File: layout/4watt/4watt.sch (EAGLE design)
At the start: 51 parts, among them IC2 FT232RL, P1 FSM4JSMA-SMD, Q1 IRF7413, Q2 IRF7413, Q3 IRF7413, Q4 IRF7413, T1 BC848, T2 BC848, T3 BC848, T4 BC848, T5 BC848, T6 BC848

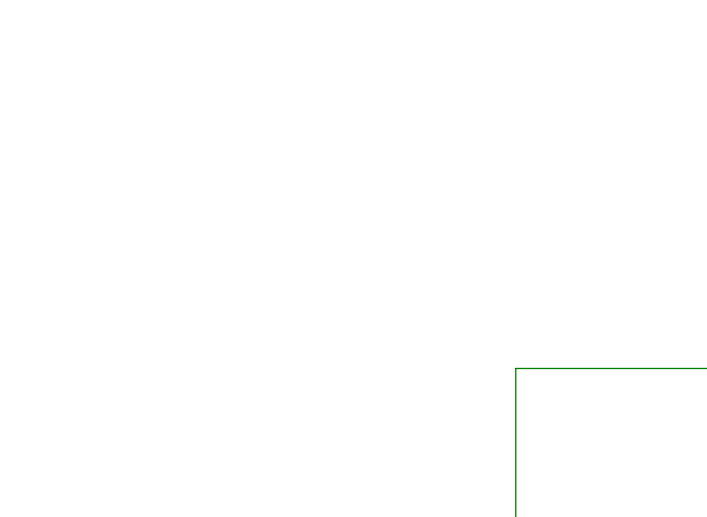
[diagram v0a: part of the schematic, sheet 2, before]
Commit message: ws28xx output and 2 additional RGBW led connectors
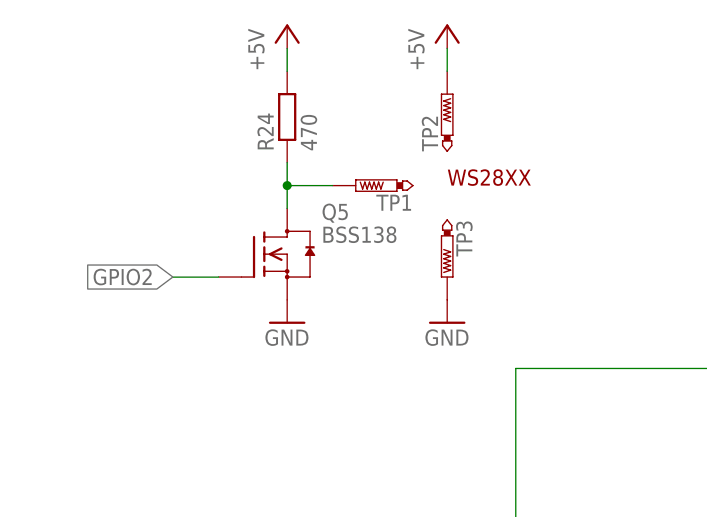
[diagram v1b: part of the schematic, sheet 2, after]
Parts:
- added Q5: BSS138, m-pad-2.1:BSS138
- added R24: 470, rcl-2:R-EU_R0603
- added TP1: PTR1B1,27, testpad:PTR1B1,27
- added TP2, TP3: PTR1B2,54, testpad:PTR1B2,54
- added X1: 1296-T10, con-leotronics:1296-T10
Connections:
- new net GPIO2: Q5.G, R21.1, U$2.GPIO2
- new net N$15: U2.PWM4, X1-2.B
- new net N$16: U2.PWM5, X1-4.B
- new net N$17: U2.PWM6, X1-6.B
- new net N$18: U2.PWM7, X1-8.B
- new net N$19: U2.PWM8, X1-1.B
- new net N$20: U2.PWM9, X1-3.B
- new net N$21: U2.PWM10, X1-5.B
- new net N$22: U2.PWM11, X1-7.B
- net +5V: now also R24.2, TP2.TP
- net GND: now also Q5.S, TP3.TP, X1-10.B, X1-9.B
- net N$6: now also Q5.D, R24.1, TP1.TP; no longer R21.1, U$2.GPIO2
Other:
- note added: "WS28XX"
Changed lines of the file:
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@@
 <part name="C9" library="rcl" deviceset="C-EU" device="C0603" value="100n"/>
 <part name="GND31" library="supply1" deviceset="GND" device=""/>
+<part name="Q5" library="m-pad-2.1" deviceset="BSS138" device=""/>
+<part name="GND32" library="supply1" deviceset="GND" device=""/>
+<part name="R24" library="rcl-2" deviceset="R-EU_" device="R0603" value="470"/>
+<part name="P+5" library="supply1" deviceset="+5V" device=""/>
+<part name="TP1" library="testpad" deviceset="PTR1" device="B1,27"/>
+<part name="TP2" library="testpad" deviceset="PTR1" device="B2,54"/>
+<part name="TP3" library="testpad" deviceset="PTR1" device="B2,54"/>
+<part name="P+7" library="supply1" deviceset="+5V" device=""/>
+<part name="GND33" library="supply1" deviceset="GND" device=""/>
+<part name="X1" library="con-leotronics" deviceset="1296-T10" device=""/>
+<part name="GND34" library="supply1" deviceset="GND" device=""/>
 </parts>
 <sheets>
@@
 <instance part="C9" gate="G$1" x="243.84" y="45.72"/>
 <instance part="GND31" gate="1" x="243.84" y="33.02"/>
+<instance part="X1" gate="-1" x="241.3" y="134.62"/>
+<instance part="X1" gate="-2" x="241.3" y="144.78"/>
+<instance part="X1" gate="-3" x="241.3" y="132.08"/>
+<instance part="X1" gate="-4" x="241.3" y="142.24"/>
+<instance part="X1" gate="-5" x="241.3" y="129.54"/>
+<instance part="X1" gate="-6" x="241.3" y="139.7"/>
+<instance part="X1" gate="-7" x="241.3" y="127"/>
+<instance part="X1" gate="-8" x="241.3" y="137.16"/>
+<instance part="X1" gate="-9" x="246.38" y="119.38"/>
+<instance part="X1" gate="-10" x="246.38" y="116.84"/>
+<instance part="GND34" gate="1" x="241.3" y="111.76"/>
 </instances>
 <busses>
@@
 <wire x1="243.84" y1="35.56" x2="243.84" y2="40.64" width="0.1524" layer="91"/>
 </segment>
+<segment>
+<pinref part="X1" gate="-10" pin="B"/>
+<pinref part="GND34" gate="1" pin="GND"/>
+<wire x1="243.84" y1="116.84" x2="241.3" y2="116.84" width="0.1524" layer="91"/>
+<wire x1="241.3" y1="116.84" x2="241.3" y2="114.3" width="0.1524" layer="91"/>
+<pinref part="X1" gate="-9" pin="B"/>
+<wire x1="243.84" y1="119.38" x2="241.3" y2="119.38" width="0.1524" layer="91"/>
+<wire x1="241.3" y1="119.38" x2="241.3" y2="116.84" width="0.1524" layer="91"/>
+<junction x="241.3" y="116.84"/>
+</segment>
 </net>
 <net name="N$12" class="0">
@@
 </segment>
 </net>
-<net name="N$6" class="0">
+<net name="GPIO2" class="0">
 <segment>
 <pinref part="U$2" gate="G$1" pin="GPIO2"/>
@@
 <pinref part="R21" gate="G$1" pin="1"/>
 <wire x1="187.96" y1="55.88" x2="187.96" y2="83.82" width="0.1524" layer="91"/>
+<wire x1="187.96" y1="55.88" x2="177.8" y2="55.88" width="0.1524" layer="91"/>
+<junction x="187.96" y="55.88"/>
+<label x="177.8" y="55.88" size="1.778" layer="95" rot="R180" xref="yes"/>
+</segment>
+</net>
+<net name="N$15" class="0">
+<segment>
+<pinref part="U2" gate="G$1" pin="PWM4"/>
+<pinref part="X1" gate="-2" pin="B"/>
+</segment>
+</net>
+<net name="N$16" class="0">
+<segment>
+<pinref part="U2" gate="G$1" pin="PWM5"/>
+<pinref part="X1" gate="-4" pin="B"/>
+</segment>
+</net>
+<net name="N$17" class="0">
+<segment>
+<pinref part="U2" gate="G$1" pin="PWM6"/>
+<pinref part="X1" gate="-6" pin="B"/>
+</segment>
+</net>
+<net name="N$18" class="0">
+<segment>
+<pinref part="U2" gate="G$1" pin="PWM7"/>
+<pinref part="X1" gate="-8" pin="B"/>
+</segment>
+</net>
+<net name="N$19" class="0">
+<segment>
+<pinref part="U2" gate="G$1" pin="PWM8"/>
+<pinref part="X1" gate="-1" pin="B"/>
+</segment>
+</net>
+<net name="N$20" class="0">
+<segment>
+<pinref part="U2" gate="G$1" pin="PWM9"/>
+<pinref part="X1" gate="-3" pin="B"/>
+</segment>
+</net>
+<net name="N$21" class="0">
+<segment>
+<pinref part="U2" gate="G$1" pin="PWM10"/>
+<pinref part="X1" gate="-5" pin="B"/>
+</segment>
+</net>
+<net name="N$22" class="0">
+<segment>
+<pinref part="U2" gate="G$1" pin="PWM11"/>
+<pinref part="X1" gate="-7" pin="B"/>
 </segment>
 </net>
@@
 <text x="154.94" y="86.36" size="1.778" layer="94">3.0V</text>
 <text x="215.9" y="86.36" size="1.778" layer="94">3.0V</text>
+<text x="53.34" y="154.94" size="1.778" layer="94">WS28XX</text>
 </plain>
 <instances>
@@
 <instance part="GND21" gate="1" x="251.46" y="48.26"/>
 <instance part="P+3" gate="1" x="134.62" y="157.48"/>
+<instance part="Q5" gate="G$1" x="33.02" y="147.32"/>
+<instance part="GND32" gate="1" x="35.56" y="139.7"/>
+<instance part="R24" gate="G$1" x="35.56" y="162.56" rot="R90"/>
+<instance part="P+5" gate="1" x="35.56" y="172.72"/>
+<instance part="TP1" gate="G$1" x="43.18" y="154.94" rot="R90"/>
+<instance part="TP2" gate="G$1" x="53.34" y="165.1"/>
+<instance part="TP3" gate="G$1" x="53.34" y="144.78" rot="R180"/>
+<instance part="P+7" gate="1" x="53.34" y="172.72"/>
+<instance part="GND33" gate="1" x="53.34" y="139.7"/>
 </instances>
 <busses>
@@
 <pinref part="GND21" gate="1" pin="GND"/>
 <wire x1="251.46" y1="58.42" x2="251.46" y2="50.8" width="0.1524" layer="91"/>
+</segment>
+<segment>
+<pinref part="Q5" gate="G$1" pin="S"/>
+<pinref part="GND32" gate="1" pin="GND"/>
+</segment>
+<segment>
+<pinref part="TP3" gate="G$1" pin="TP"/>
+<pinref part="GND33" gate="1" pin="GND"/>
 </segment>
 </net>
@@
 <pinref part="P+3" gate="1" pin="+5V"/>
 </segment>
-</net>
+<segment>
+<pinref part="R24" gate="G$1" pin="2"/>
+<pinref part="P+5" gate="1" pin="+5V"/>
+<wire x1="35.56" y1="170.18" x2="35.56" y2="167.64" width="0.1524" layer="91"/>
+</segment>
+<segment>
+<pinref part="TP2" gate="G$1" pin="TP"/>
+<pinref part="P+7" gate="1" pin="+5V"/>
+<wire x1="53.34" y1="170.18" x2="53.34" y2="167.64" width="0.1524" layer="91"/>
+</segment>
+</net>
+<net name="GPIO2" class="0">
+<segment>
+<pinref part="Q5" gate="G$1" pin="G"/>
+<wire x1="27.94" y1="144.78" x2="22.86" y2="144.78" width="0.1524" layer="91"/>
+<label x="22.86" y="144.78" size="1.778" layer="95" rot="R180" xref="yes"/>
+</segment>
+</net>
+<net name="N$6" class="0">
+<segment>
+<pinref part="R24" gate="G$1" pin="1"/>
+<pinref part="Q5" gate="G$1" pin="D"/>
+<wire x1="35.56" y1="157.48" x2="35.56" y2="154.94" width="0.1524" layer="91"/>
+<pinref part="TP1" gate="G$1" pin="TP"/>
+<wire x1="35.56" y1="154.94" x2="35.56" y2="152.4" width="0.1524" layer="91"/>
+<wire x1="35.56" y1="154.94" x2="40.64" y2="154.94" width="0.1524" layer="91"/>
+<junction x="35.56" y="154.94"/>
+</segment>
+</net>

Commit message: Bauteilbeschriftung der Platinen base und 4watt geordnet. Bestückungspläne hinzugefügt.
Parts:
- C3: value 22p -> 100n
- C4: value 22p -> 100u; device rcl:C-EUC0603 -> cap-master:CP-7343-TE-D
- C6: value 100u -> 100n; device cap-master:CP-7343-TE-D -> rcl:C-EUC0603
- C7, C8: value 100n -> 22p
- Q1: value IRF7413 -> BSS138; device transistor-fet:IRF7413 -> m-pad-2.1:BSS138
- Q5: value BSS138 -> IRF7413; device m-pad-2.1:BSS138 -> transistor-fet:IRF7413
- R10: value 3R6 -> 470; device rcl-2:R-EU_M1206 -> rcl-2:R-EU_R0603
- R16: value 3R6 -> 360; device rcl-2:R-EU_M1206 -> rcl-2:R-EU_R0603
- R18: value 360 -> 3R6; device rcl-2:R-EU_R0603 -> rcl-2:R-EU_M1206
- R19, R20, R21, R22, R23: value 10k -> 3R6; device rcl-2:R-EU_R0603 -> rcl-2:R-EU_M1206
- R24: value 470 -> 3R6; device rcl-2:R-EU_R0603 -> rcl-2:R-EU_M1206
- R5, R6, R7, R8, R9: value 3R6 -> 10k; device rcl-2:R-EU_M1206 -> rcl-2:R-EU_R0603
- TP1: value PTR1B1,27 -> PTR1B2,54; device testpad:PTR1B1,27 -> testpad:PTR1B2,54
- TP2: value PTR1B2,54 -> PTR1B1,27; device testpad:PTR1B2,54 -> testpad:PTR1B1,27
- renumbered U$2 to U$1, U$40 to X2, U2 to U1
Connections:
- net +3V3: now also C3.1, C4.+, C5.1, R3.2, R4.2, R5.2, R6.2; no longer C6.+, C7.1, C8.1, R19.2, R20.2, R21.2, R23.2
- net +5V: now also C2.1, R10.2, TP1.TP; no longer C5.1, R24.2, TP2.TP
- net GND: now also C4.-, C6.2, Q1.S, R18.1, R19.1, R20.1, R21.1, R23.1, R24.1; no longer C4.2, C6.-, Q5.S, R10.1, R11.1, R16.1, R6.1, R7.1, R8.1
- net GPIO0: now also R5.1, T1.C; no longer R23.1, T2.C
- net GPIO15: now also R9.2; no longer R22.2
- net GPIO2: now also Q1.G, R6.1; no longer Q5.G, R21.1
- net N$1: now also R7.1, T2.E; no longer R3.1, T1.E
- net N$10: now also R11.1; no longer R5.1
- net N$11: now also Q5.G, R16.2; no longer Q4.G, R18.2
- net N$12: now also C9.1; no longer C2.1
- net N$13: now also Q5.S, Q5.S1, Q5.S2, R23.2, R24.2; no longer Q4.S, Q4.S1, Q4.S2, R16.2, R17.2
- net N$14: now also Q5.D, Q5.D1, Q5.D2, Q5.D3; no longer Q4.D, Q4.D1, Q4.D2, Q4.D3
- net N$2: now also R3.1; no longer R19.1
- net N$25: now also R11.2; no longer R5.2
- net N$26: now also Q3.G; no longer Q1.G
- net N$27: now also Q3.S, Q3.S1, Q3.S2, R19.2, R20.2; no longer Q1.S, Q1.S1, Q1.S2, R6.2, R7.2
- net N$28: now also Q3.D, Q3.D1, Q3.D2, Q3.D3; no longer Q1.D, Q1.D1, Q1.D2, Q1.D3
- net N$29: now also Q4.G; no longer Q3.G
- net N$3: now also C8.1; no longer C4.1
- net N$30: now also Q4.S, Q4.S1, Q4.S2, R21.2, R22.2; no longer Q3.S, Q3.S1, Q3.S2, R10.2, R11.2
- net N$31: now also Q4.D, Q4.D1, Q4.D2, Q4.D3; no longer Q3.D, Q3.D1, Q3.D2, Q3.D3
- net N$4: now also C7.1; no longer C3.1
- net N$5: now also R8.1, T1.E; no longer R4.1, T2.E
- net N$6: now also Q1.D, R10.1, TP2.TP; no longer Q5.D, R24.1, TP1.TP
- net N$7: now also R7.2, T1.B; no longer R3.2, T2.B
- net N$8: now also R8.2, T2.B; no longer R4.2, T1.B
- net N$9: now also R17.2, R18.2; no longer R8.2, R9.2
- net RST: now also C6.1, R4.1, T2.C; no longer C9.1, R20.1, T1.C
- net W: now also R16.1; no longer R18.1
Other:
- moved on the sheet: C2, C3, C5, C7, C8, C9, Q3, Q4, R10, R11, R16, R17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
